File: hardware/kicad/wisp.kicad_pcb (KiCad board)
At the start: 4 copper layers, 60 x 80 mm, 73 parts, among them J1 USB-C, J2 Second I2C Bus, J3 mmWave UART (LD2410), J4 I2S Mic (INMP441), J5 Switched DC Output, J6 Reed/Hall Contact, J7 1-Wire Bus, J8 Analog Sensor Pad, J9 Expansion Header, Q1 MMBT3904, Q2 MMBT3904, Q3 2N7002, Q4 MMBT3904, SW1 RESET, SW2 BOOT, U1 CH340C, U2 AP63203WU-7, U3 ESP32-WROOM-32, U4 SCD41-D-R2, U5 BME680, U6 BH1750FVI-TR

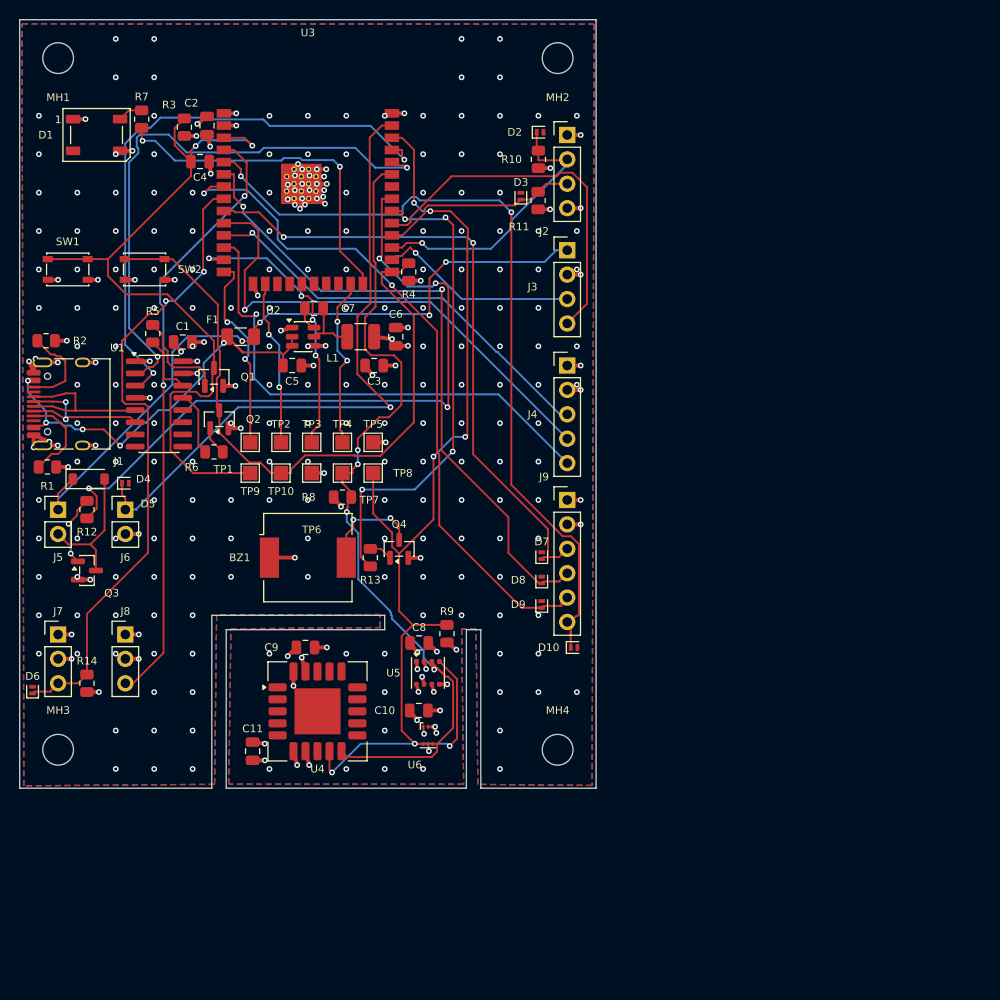
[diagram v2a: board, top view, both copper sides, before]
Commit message: Rev B: ESP32-S3, open-source VOC sensing, and generated design sources
Design review of Rev A turned up a board that would not have booted, plus a
sensor choice that could not be used without a proprietary binary blob. This
rebuilds the board around both findings.

The blocker. Rev A's auto-reset circuit drove two grounded-emitter NPNs
directly from the CH340C's active-low DTR#/RTS# outputs. Those idle HIGH, so
EN was pulled low whenever the bridge was powered and RTS was not asserted --
including on a plain USB charger. The board would have sat in reset out of the
box, and esptool's sequence would have released it only while a port was open.

Rather than patch that circuit, the MCU moves to ESP32-S3-WROOM-1-N8. Native
USB deletes the CH340C, both auto-reset transistors, their resistors and
decoupling -- nine parts and the entire bug class -- and brings USB-Serial-JTAG
so debugging needs no extra connector. It also retires the WROOM-32's
flash-voltage strapping trap on IO12, since that role belongs to IO45 on the
S3, which is not broken out.

Sensors. BME680 -> SGP41 + BME280. The BME680's gas signal is only usable
through Bosch BSEC, a closed-source blob that conflicts with the MIT licence
on /firmware and with the project's "full control over the code" premise;
Sensirion's Gas Index Algorithm is BSD-3-Clause and adds NOx alongside VOC.
Dropping the BME680 would have lost barometric pressure, so the BME280 joins
it -- not as a nicety, but because the SCD41 needs ambient pressure to
compensate its CO2 reading.

Also fixed, from the same review:
- C7 100nF, not 2.2nF (AP63203 datasheet value for the bootstrap cap)
- 10uF bulk at the module's 3V3 pin; Rev A's nearest bulk was 26mm away
- 10uF at the SCD41, which draws 205mA measurement peaks
- second 22uF at the buck output, per the datasheet's 2x22uF
- SGP41 gets its datasheet RC element: 4.7R + 1uF on VDD, own 1uF on VDDH
- USBLC6-2SC6 on D+/D-/VBUS; Rev A protected the DNP headers but not USB
- 220R series resistor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
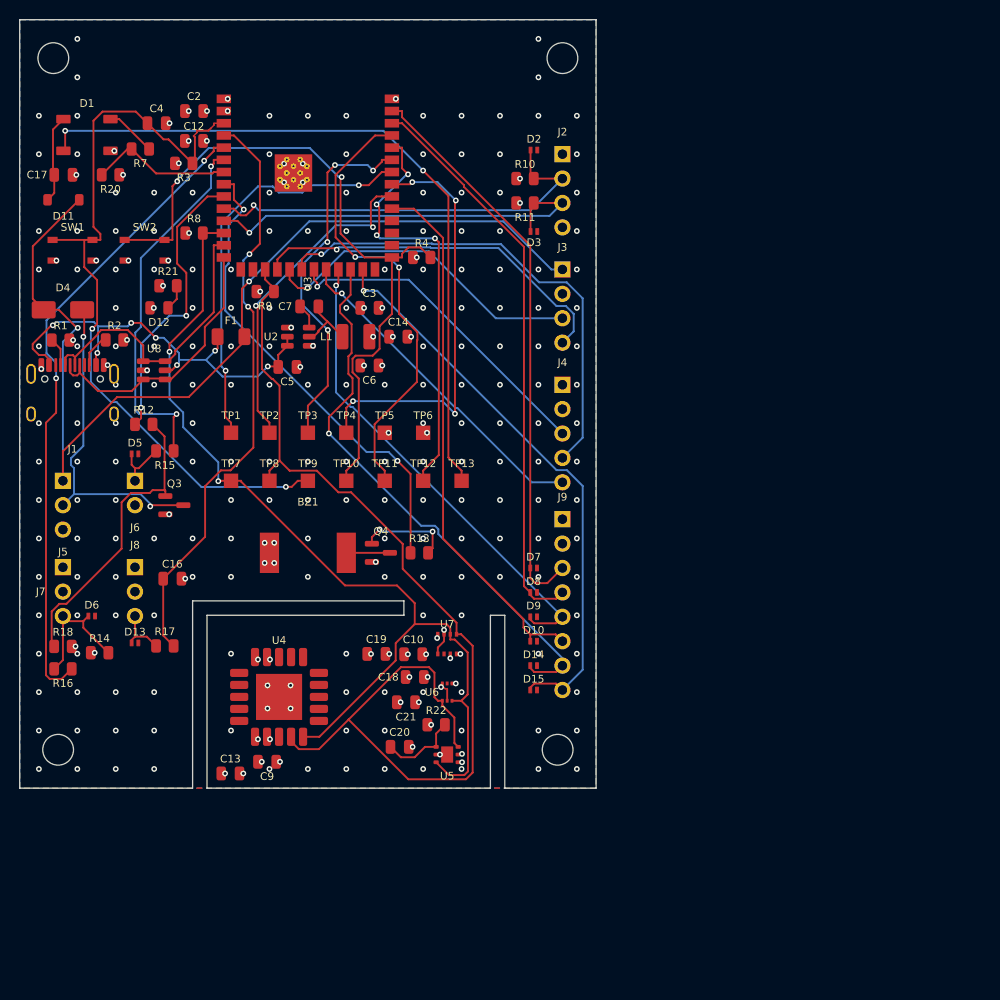
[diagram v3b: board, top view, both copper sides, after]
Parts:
- removed C1, C11, C8: 100nF, C_0805_2012Metric
- removed Q1, Q2: MMBT3904, SOT-23
- removed R5, R6: 10k, R_0805_2012Metric
- removed U1: CH340C, SOIC-16_3.9x9.9mm_P1.27mm
- added C12: 10uF, C_0805_2012Metric, F.Cu at (18.1, 12.6)
- added C13: 10uF, C_0805_2012Metric, F.Cu at (21.9, 78.5)
- added C14: 22uF, C_0805_2012Metric, F.Cu at (39.4, 33.0)
- added C16: 100nF, C_0805_2012Metric, F.Cu at (15.9, 58.2)
- added C17: 100nF, C_0805_2012Metric, F.Cu at (4.55, 16.1)
- added C18: 100nF, C_0805_2012Metric, F.Cu at (41.1, 68.4)
- added C19: 100nF, C_0805_2012Metric, F.Cu at (37.1, 66.0)
- added C20: 1uF, C_0805_2012Metric, F.Cu at (39.5, 75.7)
- added C21: 1uF, C_0805_2012Metric, F.Cu at (40.2, 71.1)
- added D11: 1N4148W, D_SOD-123, F.Cu at (4.55, 18.8)
- added D12: GREEN, LED_0805_2012Metric, F.Cu at (14.5, 30.0)
- added D13: PESD5V0L1UL, D_SOD-882, F.Cu at (12.0, 64.9)
- added D14: PESD5V0L1UL, D_SOD-882, F.Cu at (53.5, 67.2)
- added D15: PESD5V0L1UL, D_SOD-882, F.Cu at (53.5, 69.8)
- added R15: 220R, R_0805_2012Metric, F.Cu at (15.1, 44.9)
- added R16: 220R, R_0805_2012Metric, F.Cu at (4.50, 67.6)
- added R17: 220R, R_0805_2012Metric, F.Cu at (15.1, 65.2)
- added R18: 100k, R_0805_2012Metric, F.Cu at (4.50, 65.2)
- added R20: 10k, R_0805_2012Metric, F.Cu at (9.45, 16.1)
- added R21: 2.2k, R_0805_2012Metric, F.Cu at (15.4, 27.7)
- added R22: 4.7R, R_0805_2012Metric, F.Cu at (43.4, 73.4)
- added TP11: UART0_TX, TestPoint_Pad_1.5x1.5mm, F.Cu at (38.0, 48.0)
- added TP12: UART0_RX, TestPoint_Pad_1.5x1.5mm, F.Cu at (42.0, 48.0)
- added TP13: LED_DOUT, TestPoint_Pad_1.5x1.5mm, F.Cu at (46.0, 48.0)
- added U7: BME280, Bosch_LGA-8_2.5x2.5mm_P0.65mm_ClockwisePinNumbering, F.Cu at (44.5, 65.0)
- added U8: USBLC6-2SC6, SOT-23-6, F.Cu at (14.0, 36.5)
- C7: value 2.2nF -> 100nF
- D4: value 1N4148W -> SS14; footprint D_SOD-123 -> D_SMA
- J5: footprint PinHeader_1x02_P2.54mm_Vertical -> PinHeader_1x03_P2.54mm_Vertical
- J9: footprint PinHeader_1x06_P2.54mm_Vertical -> PinHeader_1x08_P2.54mm_Vertical
- MH1, MH2, MH3, MH4: value (none) -> MountingHole_M3
- Q3: value 2N7002 -> AO3400A
- TP1: value JTAG_TDI -> JTAG_MTDI
- TP2: value JTAG_TCK -> JTAG_MTCK
- TP3: value JTAG_TMS -> JTAG_MTMS
- TP4: value JTAG_TDO -> JTAG_MTDO
- U3: value ESP32-WROOM-32 -> ESP32-S3-WROOM-1-N8; footprint ESP32-WROOM-32 -> ESP32-S3-WROOM-1
- U5: value BME680 -> SGP41; footprint Bosch_LGA-8_3x3mm_P0.8mm_ClockwisePinNumbering -> Sensirion_DFN-6-1EP_2.44x2.44mm_P0.8mm_EP1.25x1.7mm
- moved R9 40.3 mm to (25.6, 28.3), turned to 0 degrees
- moved R8 31.5 mm to (18.1, 22.2)
- moved D4 17.8 mm to (4.50, 30.2)
- moved R1 13.3 mm to (4.25, 33.4)
- moved C9 12.6 mm to (25.8, 77.2)
- moved TP6 12.3 mm to (42.0, 43.0)
- moved TP7 11.6 mm to (22.0, 48.0)
- moved Q3 11.4 mm to (16.1, 50.5)
- moved TP8 10.8 mm to (26.0, 48.0)
- moved R12 10.7 mm to (12.9, 42.1), turned to 0 degrees
- moved D6 9.87 mm to (7.50, 62.1), turned to 0 degrees
- moved U5 8.73 mm to (44.5, 76.5)
- moved R2 7.12 mm to (9.87, 33.3)
- moved J8 7.07 mm to (12.0, 57.0)
- moved J7 7.02 mm to (4.50, 57.0)
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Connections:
- D1 pad 1: +3V3 -> /LED_VCC
- D1 pad 2: (no net) -> /LED_DOUT
- D10 pad 1: /EXP_IO39 -> /EXP_IO38
- D5 pad 1: /REED_IN -> /REED_EXT
- D6 pad 1: /ONEWIRE_DATA -> /ONEWIRE_EXT
- D7 pad 1: /EXP_IO33 -> /EXP_IO1
- D8 pad 1: /EXP_IO34 -> /EXP_IO2
- D9 pad 1: /EXP_IO35 -> /EXP_IO21
- J6 pad 1: /REED_IN -> /REED_EXT
- J7 pad 3: /ONEWIRE_DATA -> /ONEWIRE_EXT
- J8 pad 3: /ADC_PAD -> /ADC_PAD_EXT
- J9 pad 3: /EXP_IO33 -> /EXP_IO1
- J9 pad 4: /EXP_IO34 -> /EXP_IO2
- J9 pad 5: /EXP_IO35 -> /EXP_IO21
- J9 pad 6: /EXP_IO39 -> /EXP_IO38
- R14 pad 2: /ONEWIRE_DATA -> /ONEWIRE_EXT
- TP1 pad 1: /JTAG_TDI -> /JTAG_MTDI
- TP2 pad 1: /JTAG_TCK -> /JTAG_MTCK
- TP3 pad 1: /JTAG_TMS -> /JTAG_MTMS
- TP4 pad 1: /JTAG_TDO -> /JTAG_MTDO
- U3 pad 10: /MIC_SCK -> /SDA2
- U3 pad 11: /MIC_WS -> /SCL2
- U3 pad 12: /MIC_SD -> /SDA
- U3 pad 13: /JTAG_TMS -> /USB_DM
- U3 pad 14: /JTAG_TDI -> /USB_DP
- U3 pad 15: GND -> (no net)
- U3 pad 16: /JTAG_TCK -> (no net)
- U3 pad 17: (no net) -> /SCL
- U3 pad 18: (no net) -> /MMWAVE_RX
- U3 pad 19: (no net) -> /MMWAVE_TX
- U3 pad 20: (no net) -> /MIC_SCK
- U3 pad 21: (no net) -> /MIC_WS
- U3 pad 22: (no net) -> /MIC_SD
- U3 pad 23: /JTAG_TDO -> /EXP_IO21
- U3 pad 24: /LED_CTRL -> /EXP_IO47
- U3 pad 25: /IO0 -> /EXP_IO48
- U3 pad 26: /MMWAVE_TX -> (no net)
- U3 pad 27: /SDA2 -> /IO0
- U3 pad 28: /SCL2 -> (no net)
- U3 pad 29: /MMWAVE_RX -> (no net)
- U3 pad 30: /BUZZER_CTRL -> (no net)
- U3 pad 31: /SW_OUT_CTRL -> /EXP_IO38
- U3 pad 32: (no net) -> /JTAG_MTCK
- U3 pad 33: /SDA -> /JTAG_MTDO
- U3 pad 34: /CH_TXD -> /JTAG_MTDI
- U3 pad 35: /CH_RXD -> /JTAG_MTMS
- U3 pad 36: /SCL -> /UART0_RX
- U3 pad 37: /REED_IN -> /UART0_TX
- U3 pad 38: GND -> /EXP_IO2
- U3 pad 39: GND -> /EXP_IO1
- U3 pad 5: /EXP_IO39 -> /ONEWIRE_DATA
- U3 pad 6: /EXP_IO34 -> /REED_IN
- U3 pad 7: /EXP_IO35 -> /LED_CTRL
- U3 pad 8: /ONEWIRE_DATA -> /BUZZER_CTRL
- U3 pad 9: /EXP_IO33 -> /SW_OUT_CTRL
- U5 pad 1: GND -> /SGP_VDD
- U5 pad 2: +3V3 -> GND
- U5 pad 4: /SCL -> GND
- U5 pad 5: GND -> +3V3
- U5 pad 6: +3V3 -> /SCL
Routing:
- net /EXP_IO39: track 85.1 -> 0.00 mm, vias 2 -> 0
- net /LED_DOUT: track 0.00 -> 75.1 mm, vias 0 -> 2
- net /EXP_IO35: track 71.9 -> 0.00 mm, vias 2 -> 0
- net GND: track 87.6 -> 16.8 mm, vias 266 -> 245
- net /EXP_IO34: track 67.8 -> 0.00 mm, vias 2 -> 0
- net /EXP_IO33: track 66.4 -> 0.00 mm, vias 2 -> 0
- net /CH_RXD: track 61.7 -> 0.00 mm, vias 2 -> 0
- net /CH_TXD: track 59.8 -> 0.00 mm, vias 2 -> 0
- net /EXP_IO48: track 0.00 -> 59.6 mm, vias 0 -> 1
- net /EXP_IO2: track 0.00 -> 59.5 mm
- net /EXP_IO1: track 0.00 -> 59.4 mm
- net /EXP_IO47: track 0.00 -> 58.5 mm, vias 0 -> 1
- net /EXP_IO38: track 0.00 -> 56.0 mm
- net /EXP_IO21: track 0.00 -> 50.2 mm, vias 0 -> 1
- net /UART0_TX: track 0.00 -> 47.2 mm, vias 0 -> 2
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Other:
- outline, holes or cut-outs redrawn
